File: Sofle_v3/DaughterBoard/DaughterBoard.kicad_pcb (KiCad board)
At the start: 2 copper layers, 26.2 x 19.5 mm, 2 parts, among them SW1 RotaryEncoder_Switch, SW2 RotaryEncoder_Switch

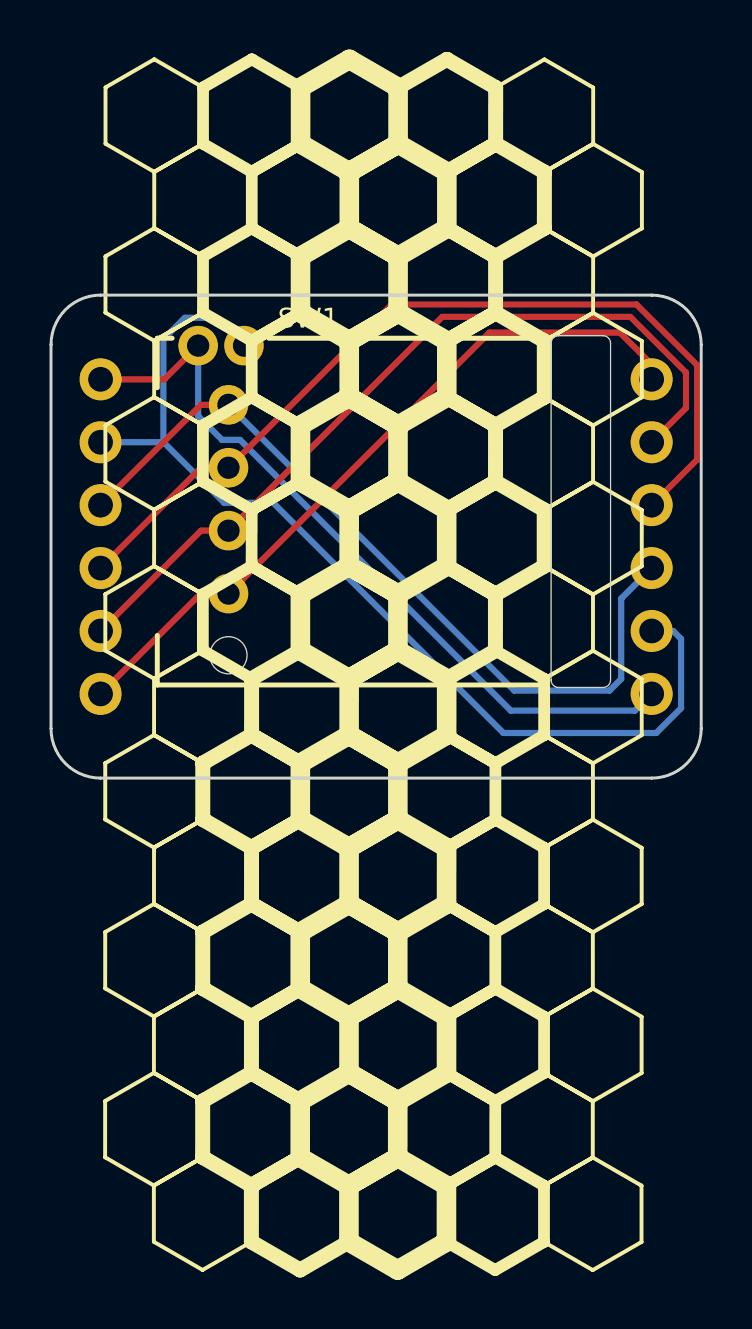
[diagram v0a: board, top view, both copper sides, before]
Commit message: Design: Fixed daughterboard pinout/Made it configurable
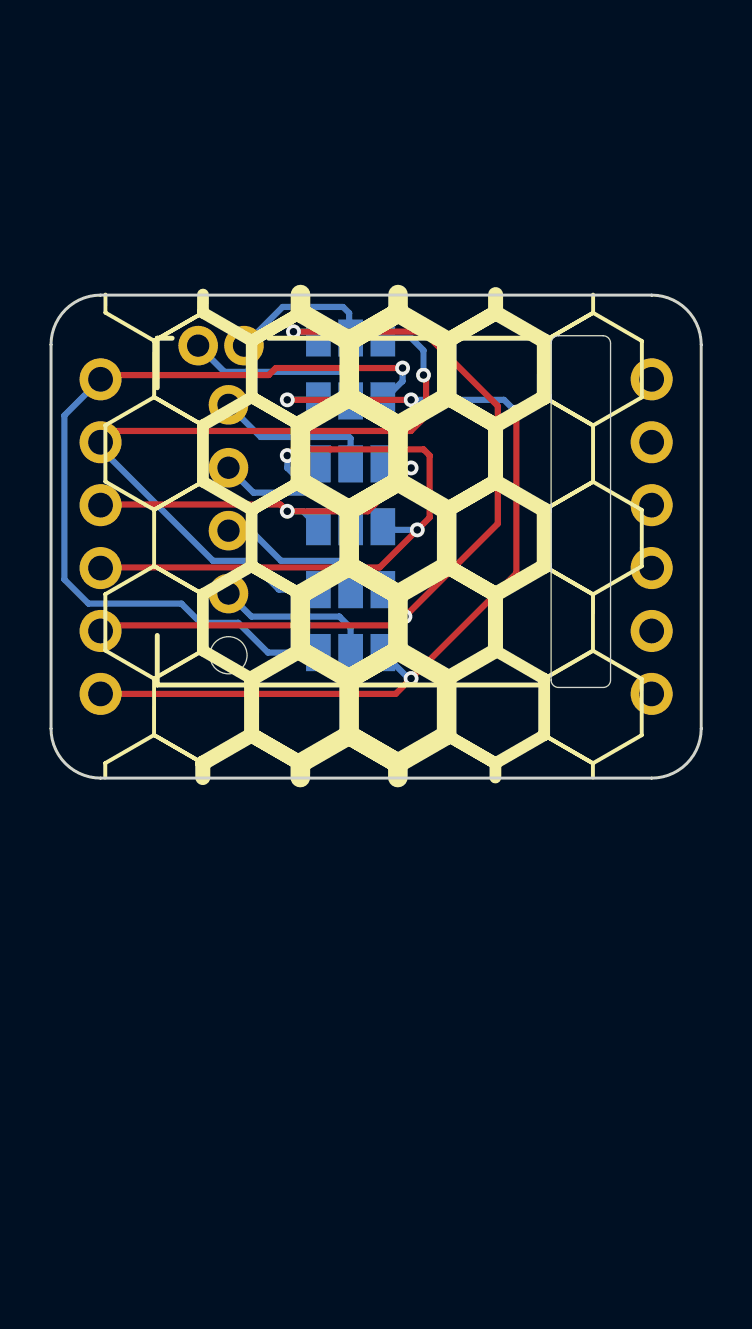
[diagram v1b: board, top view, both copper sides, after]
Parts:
- added JP1: Jumper_3_Open, Jumper:SolderJumper-3_P1.3mm_Open_Pad1.0x1.5mm, B.Cu at (146.7, 76.6)
- added JP2: Jumper_3_Open, Jumper:SolderJumper-3_P1.3mm_Open_Pad1.0x1.5mm, B.Cu at (146.7, 74.0)
- added JP3: Jumper_3_Open, Jumper:SolderJumper-3_P1.3mm_Open_Pad1.0x1.5mm, B.Cu at (146.7, 79.1)
- added JP4: Jumper_3_Open, Jumper:SolderJumper-3_P1.3mm_Open_Pad1.0x1.5mm, B.Cu at (146.7, 86.7)
- added JP5: Jumper_3_Open, Jumper:SolderJumper-3_P1.3mm_Open_Pad1.0x1.5mm, B.Cu at (146.7, 84.2)
- added JP6: Jumper_3_Open, Jumper:SolderJumper-3_P1.3mm_Open_Pad1.0x1.5mm, B.Cu at (146.7, 81.7)
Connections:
- SW1 pad A: Net-(SW1-PadA) -> /E_A
- SW1 pad B: Net-(SW1-PadB) -> /E_B
- SW1 pad C: Net-(SW1-PadC) -> /E_C
- SW1 pad D: Net-(SW1-PadD) -> /E_D
- SW1 pad S1: Net-(SW1-PadS1) -> /E_S1
- SW1 pad S2: Net-(SW1-PadS2) -> /E_S2
- SW2 pad A: Net-(SW1-PadA) -> /A
- SW2 pad B: Net-(SW1-PadB) -> /B
- SW2 pad C: Net-(SW1-PadC) -> /C
- SW2 pad D: Net-(SW1-PadD) -> /D
- SW2 pad S1: Net-(SW1-PadS1) -> /S1
- SW2 pad S2: Net-(SW1-PadS2) -> /S2
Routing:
- net Net-(SW1-PadS2): track 41.1 -> 0.00 mm
- net /D: track 0.00 -> 37.6 mm, vias 0 -> 4
- net Net-(SW1-PadB): track 35.9 -> 0.00 mm
- net /C: track 0.00 -> 34.6 mm, vias 0 -> 2
- net /S1: track 0.00 -> 34.2 mm, vias 0 -> 1
- net Net-(SW1-PadC): track 33.2 -> 0.00 mm
- net Net-(SW1-PadA): track 32.7 -> 0.00 mm
- net Net-(SW1-PadS1): track 30.9 -> 0.00 mm
- net /S2: track 0.00 -> 29.5 mm, vias 0 -> 1
- net Net-(SW1-PadD): track 29.4 -> 0.00 mm
- net /B: track 0.00 -> 26.1 mm, vias 0 -> 2
- net /A: track 0.00 -> 16.1 mm, vias 0 -> 2
- net /E_S1: track 0.00 -> 7.66 mm
- net /E_A: track 0.00 -> 6.52 mm
- net /E_D: track 0.00 -> 6.50 mm
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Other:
- rule pad_to_mask_clearance: 0 -> 0.2
- board text added: "EVQWGD001 Daughterboard v2"
- board text added: "L"
- board text added: "R"

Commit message: [Fix] Fixed wrong wiring of Daughter board
To be precice, the main pcb has a wrong layout but it is cheaper
and easier to fix the wiring on the daughter board. This is now
how it alaways was meant to be ;)
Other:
- rule pad_to_mask_clearance: 0.2 -> 0
- board text added: "JLCJLCJLCJLC"
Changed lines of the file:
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@@
       (dielectric_constraints no)
     )
-    (pad_to_mask_clearance 0.2)
+    (pad_to_mask_clearance 0)
     (aux_axis_origin 135.128 81.788)
     (grid_origin 135.128 81.788)
     (pcbplotparams
-      (layerselection 0x00410fc_ffffffff)
+      (layerselection 0x00010fc_ffffffff)
       (plot_on_all_layers_selection 0x0000000_00000000)
       (disableapertmacros false)
       (usegerberextensions true)
-      (usegerberattributes true)
-      (usegerberadvancedattributes true)
+      (usegerberattributes false)
+      (usegerberadvancedattributes false)
       (creategerberjobfile false)
       (dashed_line_dash_ratio 12.000000)
@@
       (psa4output false)
       (plotreference true)
-      (plotvalue true)
+      (plotvalue false)
       (plotinvisibletext false)
       (sketchpadsonfab false)
@@
         (effects (font (size 0.8 0.8) (thickness 0.2)))
     )
-    (fp_text user "${REFERENCE}" (at 12.5 0) (layer "F.Fab")
+    (fp_text user "${REFERENCE}" (at 12.5 0) (layer "F.Fab") hide
         (effects (font (size 1 1) (thickness 0.15)))
     )
@@
   (gr_line (start 150.576542 60.524632) (end 152.546116 59.388639)
     (stroke (width 0.60577) (type solid)) (layer "User.1"))
-  (gr_text "R" (at 148.628 89.788) (layer "B.SilkS")
+  (gr_text "R" (at 148.5 90) (layer "B.SilkS")
     (effects (font (size 1 1) (thickness 0.15)) (justify left bottom mirror))
   )
-  (gr_text "EVQWGD001\nDaughterboard v2" (at 154.128 89.288 90) (layer "B.SilkS")
-    (effects (font (size 1.2 1.2) (thickness 0.3) bold) (justify left bottom))
+  (gr_text "EVQWGD001\nDaughterboard v2" (at 150.628 89.788 -90) (layer "B.SilkS")
+    (effects (font (size 1.2 1.2) (thickness 0.3) bold) (justify left bottom mirror))
   )
-  (gr_text "L" (at 145.628 89.788) (layer "B.SilkS")
+  (gr_text "JLCJLCJLCJLC" (at 137.628 88.788 -90) (layer "B.SilkS")
+    (effects (font (size 1.5 1.5) (thickness 0.3) bold) (justify left bottom mirror))
+  )
+  (gr_text "L" (at 145.5 90) (layer "B.SilkS")
     (effects (font (size 1 1) (thickness 0.15)) (justify left bottom mirror))
   )
